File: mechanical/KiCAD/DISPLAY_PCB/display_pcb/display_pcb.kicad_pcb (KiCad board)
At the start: 4 copper layers, 49.9 x 56.5 mm, 50 parts, among them J1 USB_C_Receptacle_USB2.0_16P, J2 Conn_01x18_Socket, J3 Conn_01x01_Pin, J4 Conn_01x01_Pin, J5 Conn_01x02_Pin, Q1 AO3401A, U1 ESP32-S3-WROOM-1, U3 USBLC6-2P6, U4 TP4056-42-ESOP8, U5 TLV75733PDBV

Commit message: PCBs should be finished, they can be ordered. The plan was to finish the PCB design about a week ago. I already have the display and got two ESP devboard so i can start the software and test it.
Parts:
- C5: value 20uF -> 22uF
- C6: footprint Capacitor_SMD:C_1206_3216Metric -> Capacitor_SMD:C_0805_2012Metric
- R5, R6, R7, R9: footprint Resistor_SMD:R_0805_2012Metric -> Resistor_SMD:R_0603_1608Metric
- moved J4 10.1 mm to (131.5, 76.8)
- moved C13 6.97 mm to (105.0, 68.7), turned to -90 degrees
- moved J3 3.05 mm to (131.6, 72.7)
- moved D1 1.13 mm to (95.2, 73.9)
- moved D3 1.13 mm to (95.3, 76.2)
- moved R5 1.13 mm to (99.3, 73.9)
- moved R6 1.13 mm to (99.3, 76.2)
- moved D4 1.13 mm to (95.3, 78.6)
- moved R7 1.13 mm to (99.3, 78.6)
- turned C4 to -90 degrees
- turned EN1 to 90 degrees
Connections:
- J5 pad 2: BTR - -> GND
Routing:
- net +5V: track 47.4 -> 57.9 mm, vias 8 -> 7
- net BTR +: track 38.8 -> 43.6 mm
- net Net-(J4-Pin_1): track 10.7 -> 15.2 mm
- net Net-(J3-Pin_1): track 10.7 -> 14.9 mm
- net BTR CHRG: track 26.1 -> 28.4 mm
- net GREEN_LED: track 7.86 -> 9.91 mm, vias 2 -> 0
- net BLUE_LED: track 9.10 -> 11.0 mm, vias 2 -> 0
- net +3.3V: track 81.1 -> 79.3 mm, vias 7 -> 4
- net RED_LED: track 7.25 -> 9.00 mm, vias 2 -> 0
- net BOOT: track 17.7 -> 19.2 mm
- net GND: track 0.00 -> 0.45 mm, vias 47 -> 64
- net Net-(D2-A1): vias 6 -> 0
- net Net-(F1-Pad1): vias 2 -> 0

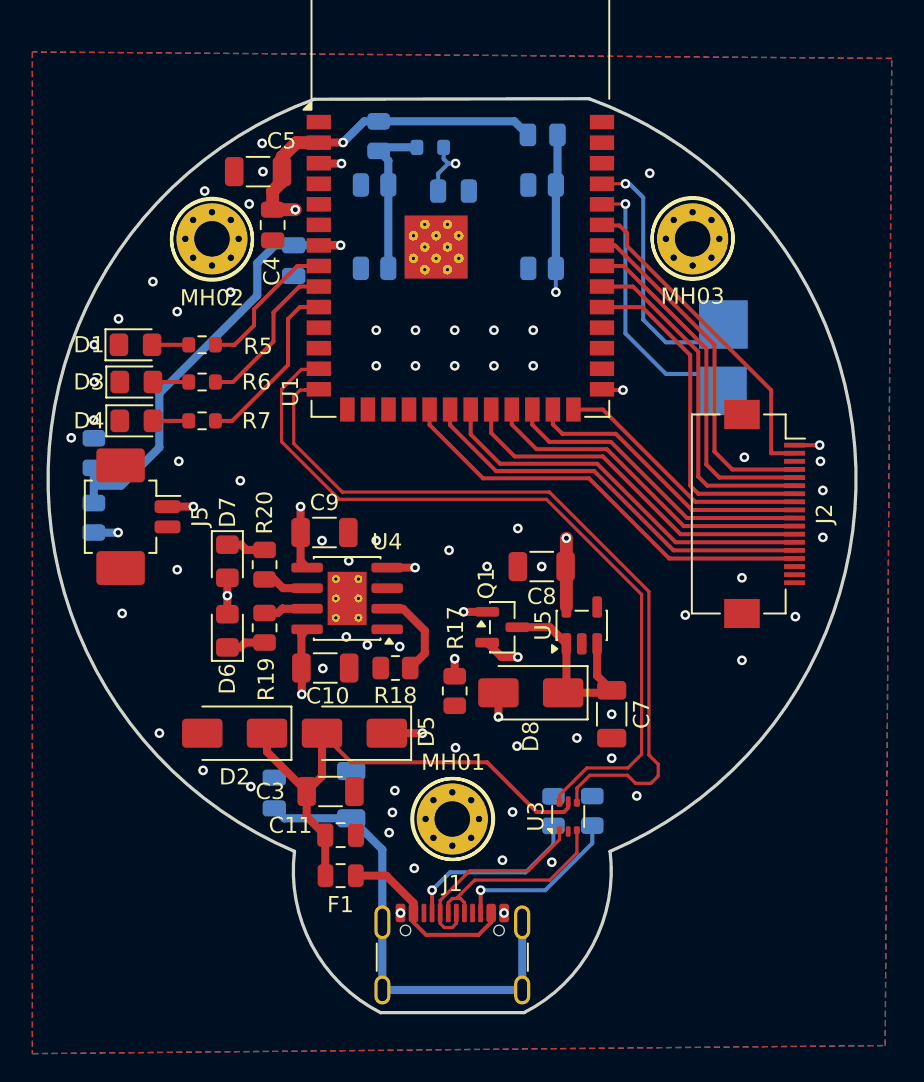
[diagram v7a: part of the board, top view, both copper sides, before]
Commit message: Small changes due to via and silkscreen overlaps, moved every via-in-pad seperately from soldering pad. PCBs have been ordered. Some problems occured with the buttons since the ones i chose had a 5th mounting pin which was not present on the PCB. Also they asked about the button polarity and placement.Everything was corrected and the order moved to production.
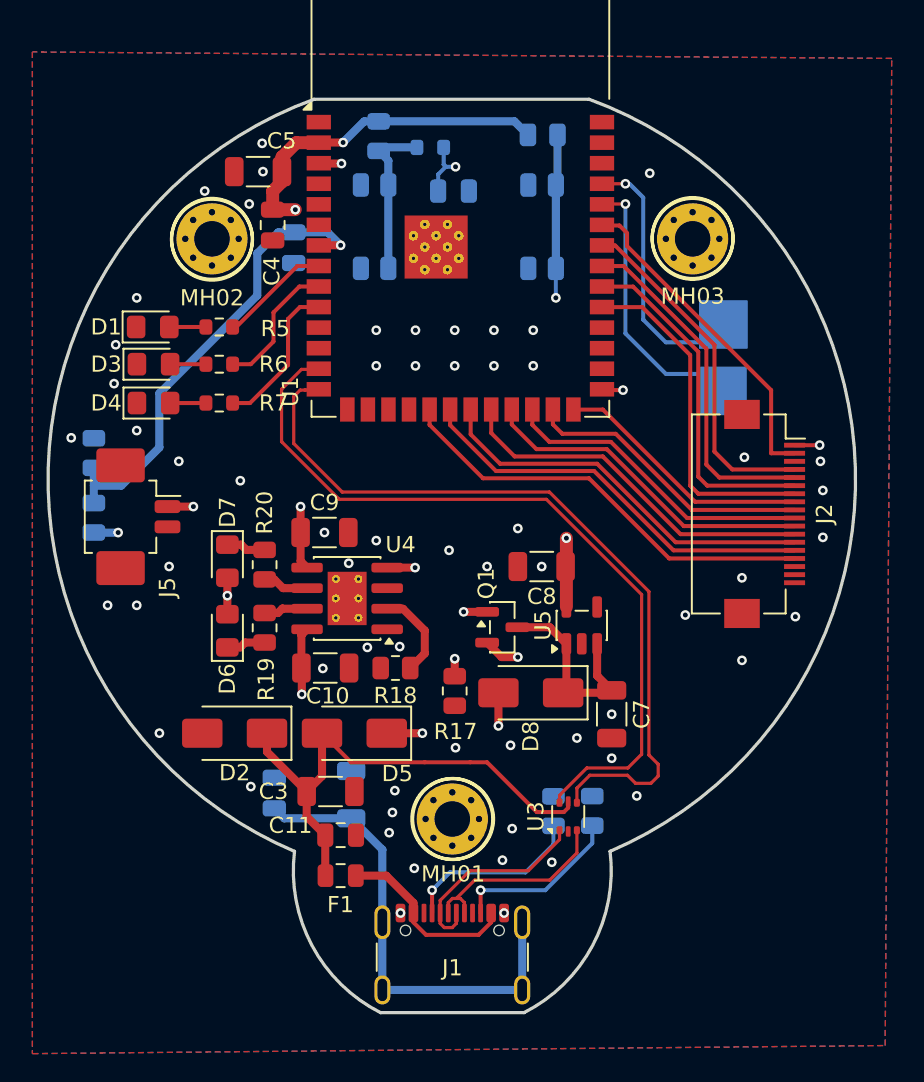
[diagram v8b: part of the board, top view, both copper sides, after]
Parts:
- moved D1 1.53 mm to (96.3, 72.8)
- moved D3 1.53 mm to (96.3, 75.1)
- moved R5 1.53 mm to (100.4, 72.8)
- moved R6 1.53 mm to (100.4, 75.1)
- moved D4 1.53 mm to (96.3, 77.5)
- moved R7 1.53 mm to (100.4, 77.5)
- moved C13 0.80 mm to (105.0, 67.9)
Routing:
- net RED_LED: track 9.00 -> 6.89 mm
- net GREEN_LED: track 9.91 -> 8.39 mm
- net BLUE_LED: track 11.0 -> 9.51 mm
- net BTR CHRG: track 28.4 -> 29.4 mm
- net GND: vias 64 -> 60
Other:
- board size 49.9 x 56.5 mm -> 49.9 x 56.4 mm
